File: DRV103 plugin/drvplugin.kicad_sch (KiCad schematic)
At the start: 16 parts, among them J1 Conn_02x05_Odd_Even, U1 PC817, U2 DRV103H

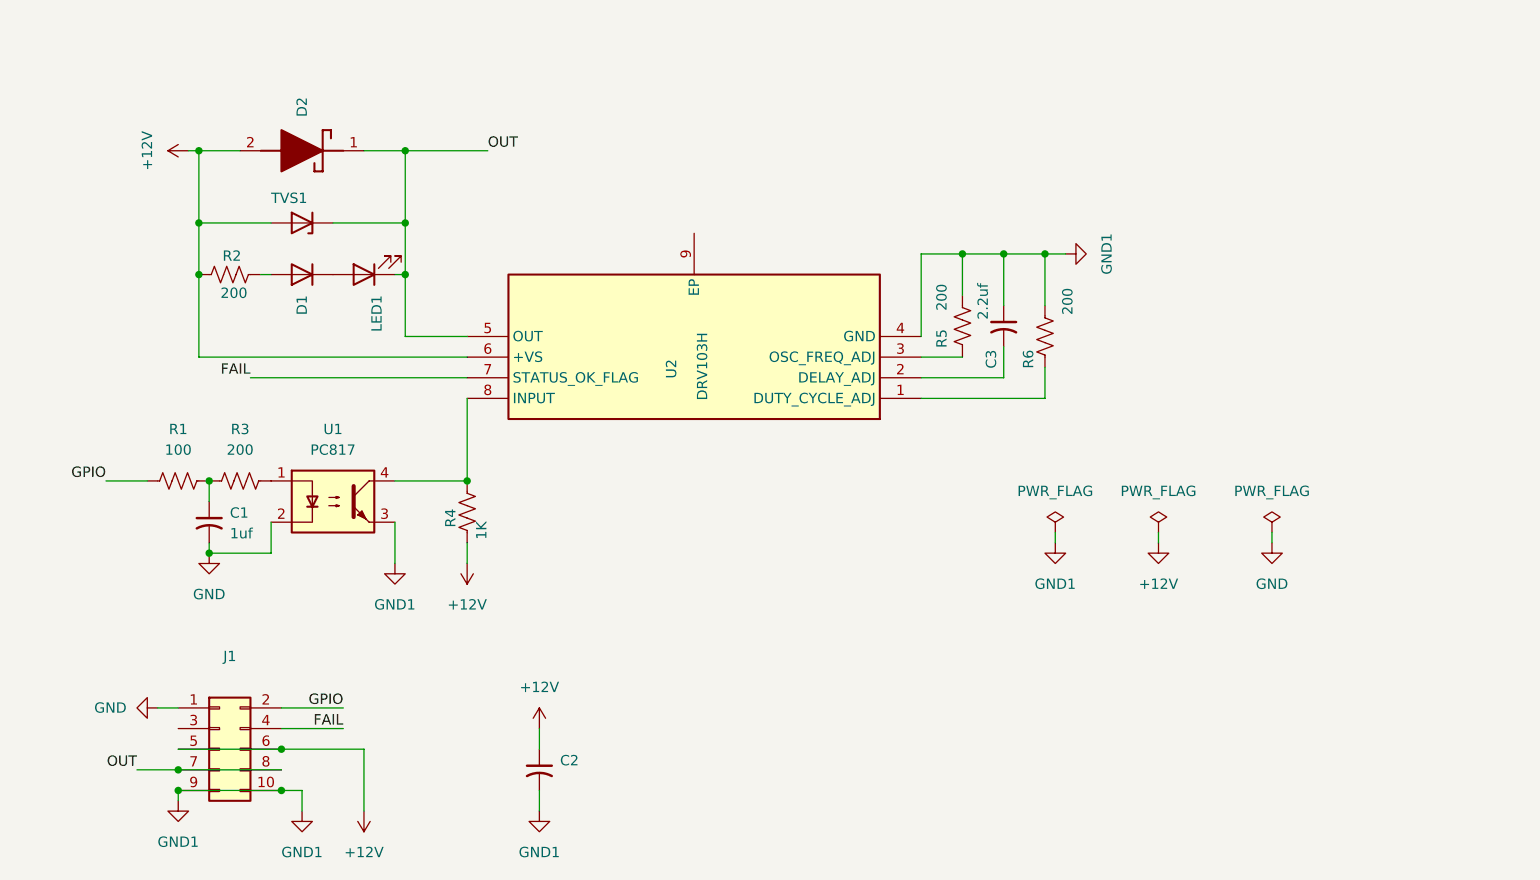
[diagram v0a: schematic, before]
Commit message: fixes for power switch, also looks like KiCad might have boned some of our pinouts
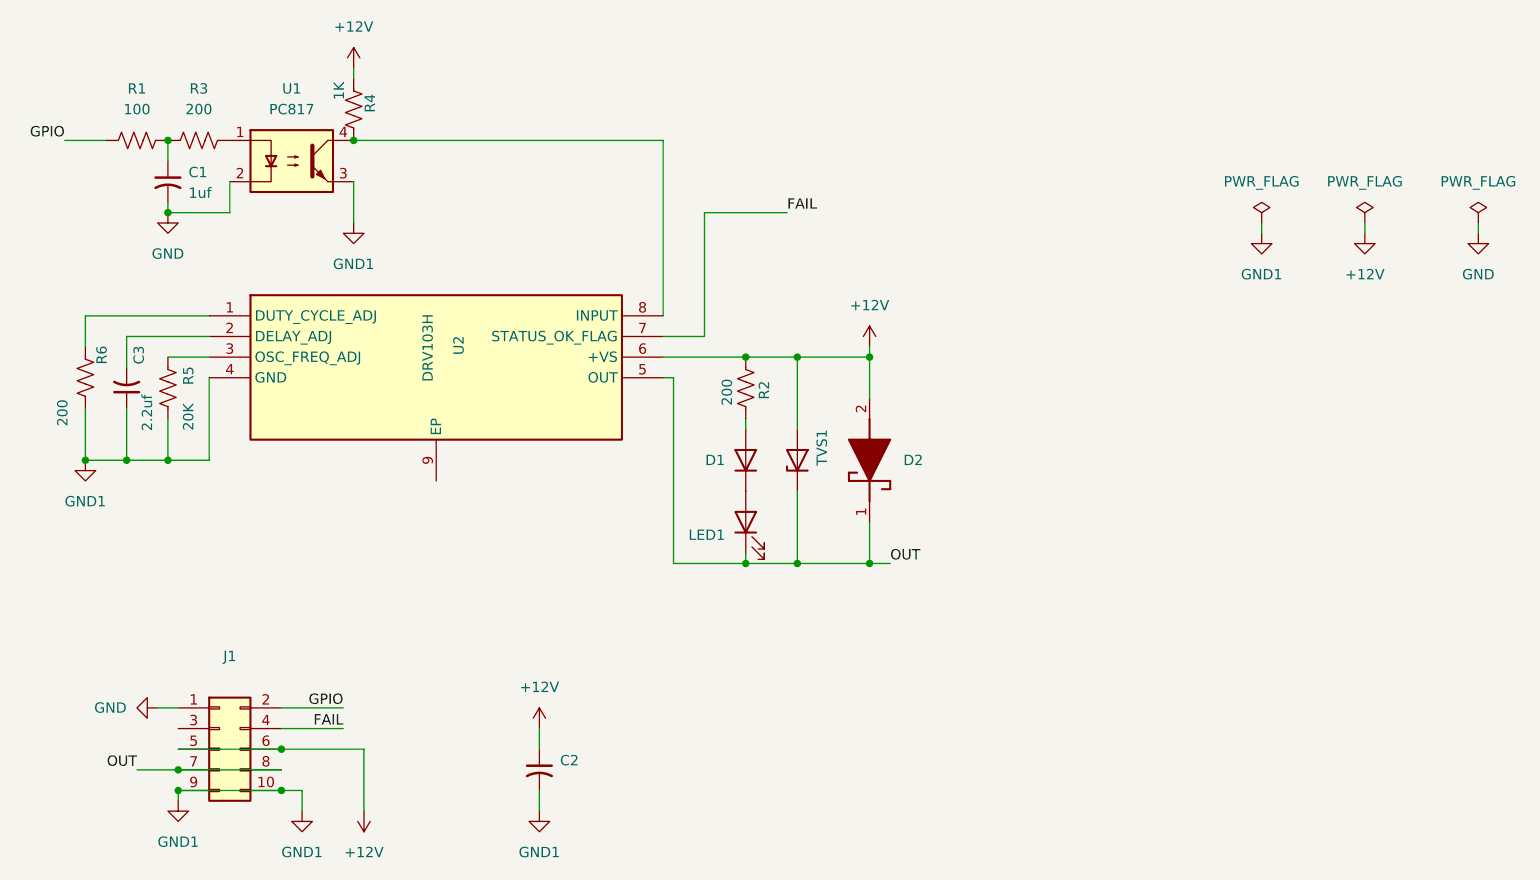
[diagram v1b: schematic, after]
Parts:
- R5: value 200 -> 20K
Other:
- moved on the sheet: C1, C3, D1, D2, LED1, R1, R2, R3, R4, R5, R6, TVS1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
